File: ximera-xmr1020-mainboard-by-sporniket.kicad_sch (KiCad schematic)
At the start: 0 parts

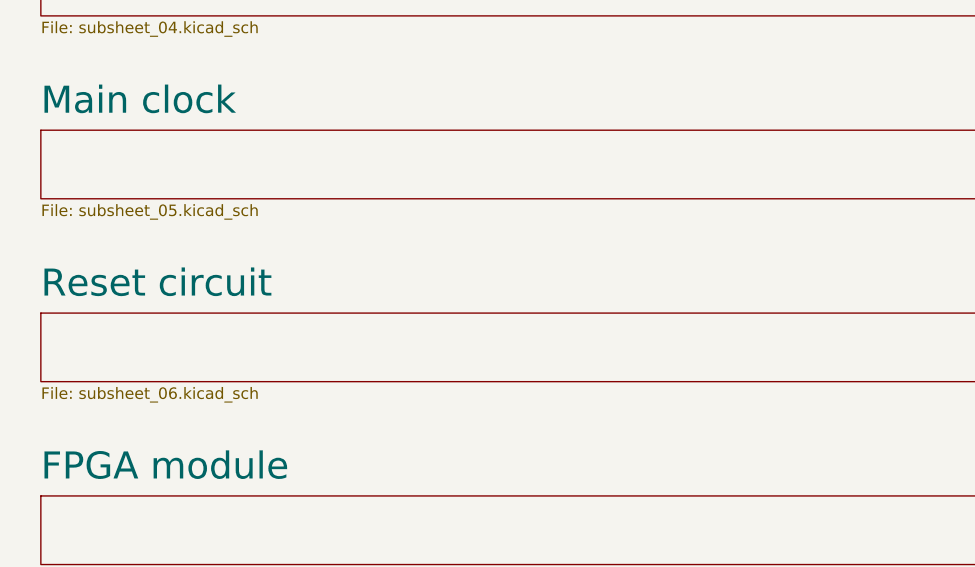
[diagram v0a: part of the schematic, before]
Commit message: added todo in schematics
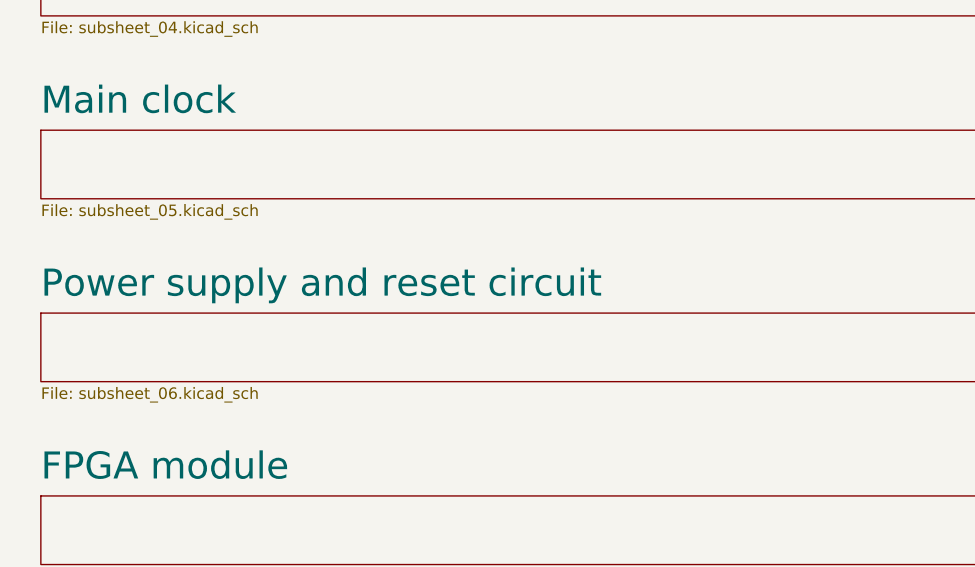
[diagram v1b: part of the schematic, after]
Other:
- sheet Reset circuit renamed Power supply and reset circuit
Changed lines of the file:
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@@
     (stroke (width 0.1524) (type solid))
     (fill (color 0 0 0 0.0000))
-    (property "Sheetname" "Reset circuit" (at 25.4 163.5234 0)
+    (property "Sheetname" "Power supply and reset circuit" (at 25.4 163.5234 0)
       (effects (font (size 3 3)) (justify left bottom))
     )

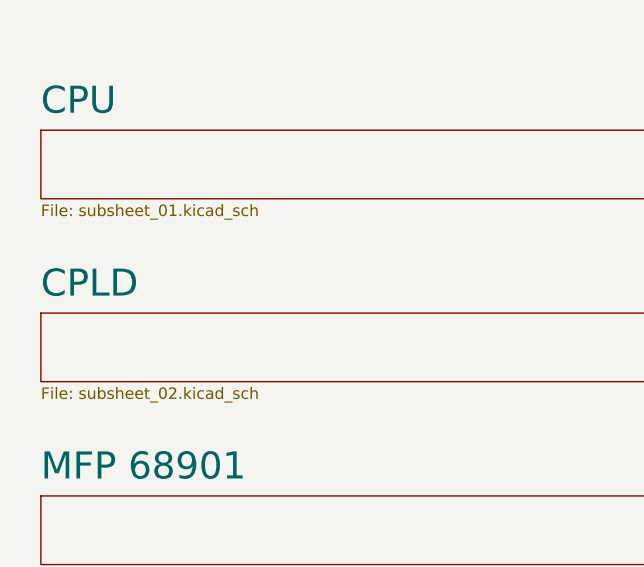
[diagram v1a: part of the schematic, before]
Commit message: CPU : pulled up addr24..addr31 ; CPLD : started
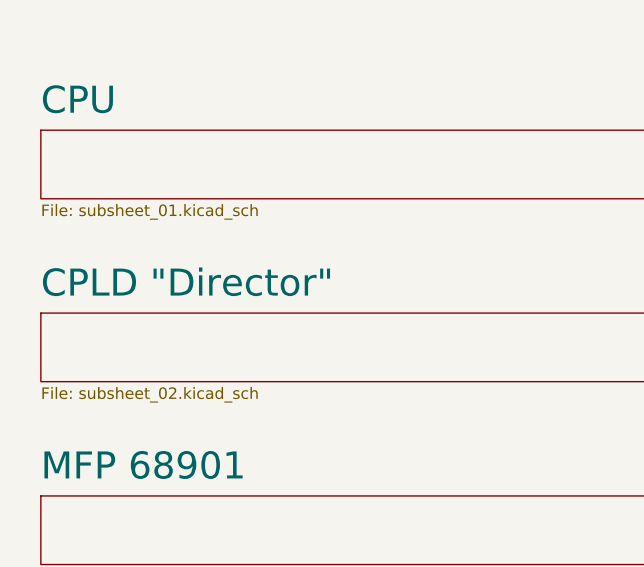
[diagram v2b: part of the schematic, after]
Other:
- sheet CPLD renamed CPLD "Director"
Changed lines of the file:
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@@
     (stroke (width 0.1524) (type solid))
     (fill (color 0 0 0 0.0000))
-    (property "Sheetname" "CPLD" (at 25.4 82.2434 0)
+    (property "Sheetname" "CPLD \"Director\"" (at 25.4 82.2434 0)
       (effects (font (size 3 3)) (justify left bottom))
     )
